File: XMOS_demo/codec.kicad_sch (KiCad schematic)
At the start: 1 part, among them U2 CS4271

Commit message: Lots of sch work
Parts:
- added C37, C39, C45, C47, C50: 100n, Capacitor_SMD:C_0603_1608Metric, symbol Device:C_Small
- added C43: 1u, Capacitor_SMD:CP_Elec_4x5.4, symbol Device:C_Polarized_Small
- added C44: 47u, Capacitor_SMD:CP_Elec_6.3x5.7, symbol Device:C_Polarized_Small
- added C46, C48, C49: 1u, Capacitor_SMD:C_0603_1608Metric, symbol Device:C_Small
- added R25, R28, R30, R31, R32, R33, R34: 0R, Resistor_SMD:R_0603_1608Metric, symbol Device:R_Small
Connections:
- net P3V3: now reaches U2.10 (VL)
- net P3V3: now also U2.9 (VD), C47.1, C48.1, C49.1, C50.1
- net ~{RST}: now reaches U2.14 (~{RST})
- net ~{RST}: now also R34.2
- net VQ1: now reaches U2.15 (VQ1)
- net VQ1: now also C39.1, C43.1
- net VQ2: now reaches U2.16 (VQ2)
- net AIN_A: now reaches U2.17 (AINA)
- net AIN_B: now reaches U2.18 (AINB)
- net VQ3: now reaches U2.19 (VQ3)
- net at U2.20 (VA): now also C45.1, C46.1, R25.1
- net GND: now reaches U2.21 (AGND)
- net GND: now also U2.8 (DGND), C37.2, C39.2, C43.2, C44.2, C45.2, C46.2, C47.2, C48.2, C49.2, C50.2
- net at U2.22 (FILT+): now also C37.1, C44.1
- net ~{MUTE}: now reaches U2.23 (~{AMUTEC})
- net OUT_A-: now reaches U2.24 (AOUTA-)
- net OUT_A+: now reaches U2.25 (AOUTA+)
- net OUT_B+: now reaches U2.26 (AOUTB+)
- net OUT_B-: now reaches U2.27 (AOUTB-)
- net MCLK: now reaches U2.3 (MCLK)
- net MCLK: now also R28.2
- net LRCK: now reaches U2.4 (LRCK)
- net LRCK: now also R30.2
- net SCLK: now reaches U2.5 (SCLK)
- net SCLK: now also R31.2
- net SDOUT: now reaches U2.6 (SDOUT(M/~{S}))
- net SDOUT: now also R33.2
- net SDIN: now reaches U2.7 (SDIN)
- net SDIN: now also R32.2
- new net CODEC_LRCK: R30.1
- new net CODEC_MCLK: R28.1
- new net CODEC_SCLK: R31.1
- new net CODEC_SDIN: R32.1
- new net CODEC_SDOUT: R33.1
- new net CODEC_~{RST}: R34.1
- new net P5V0: R25.2
- no-connect marks 0 -> 1
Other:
- note added: "TODO: DNP crystal, M/~{S} selection"
- moved on the sheet: U2

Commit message: sch work, pcb import and initial board outline
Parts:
- added C52, C53: 39p, Capacitor_SMD:C_0603_1608Metric, symbol Device:C_Small
- added R38, R40: 0R, Resistor_SMD:R_0603_1608Metric, symbol Device:R_Small
- added R39: 47k, Resistor_SMD:R_0603_1608Metric, symbol Device:R_Small
- added R43, R44: 680R, Resistor_SMD:R_0603_1608Metric, symbol Device:R_Small
- added Y2: 24.576M, Crystal:Crystal_SMD_2520-4Pin_2.5x2.0mm, symbol _Oscillator:Crystal_24M
- R25: value 0R -> 100k; Tolerance (none) -> 1%
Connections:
- net GND: now also R25.2, C52.2, C53.2, R38.1, R44.2, Y2.2 (G), Y2.4 (G)
- net P3V3: now also R39.1, R43.1
- net P5V0: now also R40.2; no longer R25.2
- net SDOUT: now also R39.2
- net ~{RST}: now also R25.1
- net at C45.1, C46.1, U2.20 (VA): now also R40.1; no longer R25.1
- net at U2.1 (XT0): now also C52.1, Y2.3
- net SCL: now reaches U2.11 (SCL/CCLK(M0))
- net SDA: now reaches U2.12 (SDA/CDIN(M1))
- net AD0: now reaches U2.13 (AD0/~{CS}(I2S/~{LJ}))
- net AD0: now also R43.2, R44.1
- net at U2.2 (XTI): now also C53.1, R38.2, Y2.1
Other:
- note removed: "TODO: DNP crystal, M/~{S} selection"
- moved on the sheet: C37, C39, C43, C44, R28, R30, R31, R32, R33, R34

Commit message: sch mostly finished, needs tp, pcb component layout started
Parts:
- renumbered C49 to C45, C50 to C46, C48 to C47, C47 to C48, C45 to C49, C46 to C50, C37 to C51, C44 to C52, C39 to C53, C43 to C54, C52 to C55, C53 to C56, R40 to R37, R34 to R38, R25 to R39, R28 to R40, R39 to R41, R30 to R42, R31 to R43, R33 to R44, R32 to R45, R43 to R46, R44 to R47, R38 to R48, U2 to U8

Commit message: finished sch, pcb work
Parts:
- renumbered R37 to R35, R38 to R36, R39 to R37, R40 to R38, R41 to R39, R42 to R40, R43 to R41, R44 to R42, R45 to R43, R46 to R44, R47 to R45, R48 to R46
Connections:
- net CODEC_MCLK is gone; now on net MCLK: R38.1
- net CODEC_LRCK renamed I2S_LRCK
- net CODEC_SCLK renamed I2S_SCLK
- net CODEC_SDIN renamed I2S_DAC
- net CODEC_SDOUT renamed I2S_ADC

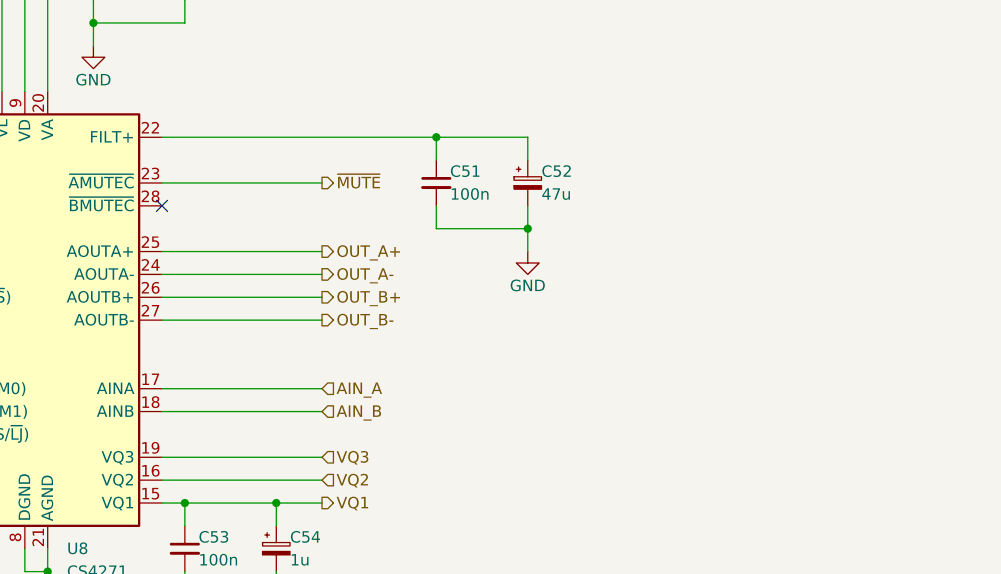
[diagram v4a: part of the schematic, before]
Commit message: sch work changes (jumpers, connectors, tp)
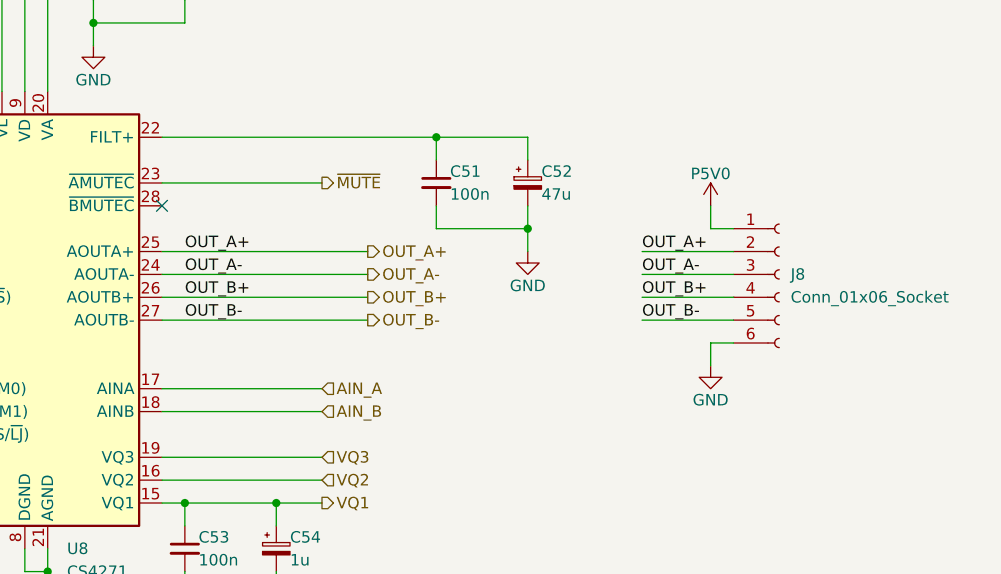
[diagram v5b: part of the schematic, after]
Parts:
- added J8: Conn_01x06_Socket, Connector_PinHeader_2.54mm:PinHeader_1x06_P2.54mm_Vertical, symbol Connector:Conn_01x06_Socket
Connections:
- net GND: now also J8.6 (Pin_6)
- net OUT_A+: now also J8.2 (Pin_2)
- net OUT_A-: now also J8.3 (Pin_3)
- net OUT_B+: now also J8.4 (Pin_4)
- net OUT_B-: now also J8.5 (Pin_5)
- net P5V0: now also J8.1 (Pin_1)

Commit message: merge
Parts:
- C46, C48, C49: footprint Capacitor_SMD:C_0603_1608Metric -> Capacitor_SMD:C_0402_1005Metric
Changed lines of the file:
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@@
 			)
 		)
-		(property "Footprint" "Capacitor_SMD:C_0603_1608Metric"
+		(property "Footprint" "Capacitor_SMD:C_0402_1005Metric"
 			(at 142.24 71.12 0)
 			(effects
@@
 			)
 		)
-		(property "Footprint" "Capacitor_SMD:C_0603_1608Metric"
+		(property "Footprint" "Capacitor_SMD:C_0402_1005Metric"
 			(at 157.48 71.12 0)
 			(effects
@@
 			)
 		)
-		(property "Footprint" "Capacitor_SMD:C_0603_1608Metric"
+		(property "Footprint" "Capacitor_SMD:C_0402_1005Metric"
 			(at 121.92 71.12 0)
 			(effects

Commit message: pcb routing
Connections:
- net VQ3 is gone; now on net VQ2_3: U8.19 (VQ3)
- net VQ2 renamed VQ2_3
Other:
- moved on the sheet: C45, C46, C47, C48, C49, C50, C51, C52, C53, C54, C55, C56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

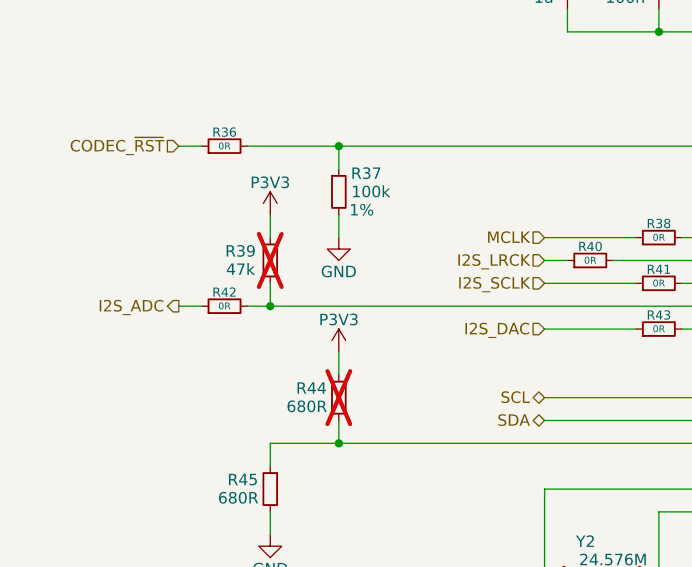
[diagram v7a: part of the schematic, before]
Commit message: I2S config sch page added
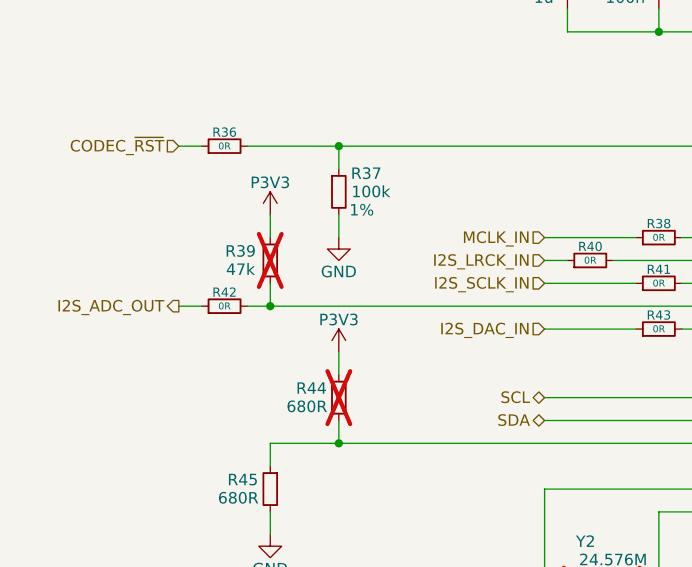
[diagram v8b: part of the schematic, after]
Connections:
- net MCLK: no longer R38.1
- net I2S_ADC renamed I2S_ADC_OUT
- net I2S_DAC renamed I2S_DAC_IN
- net I2S_LRCK renamed I2S_LRCK_IN
- net I2S_SCLK renamed I2S_SCLK_IN
- new net MCLK_IN: R38.1
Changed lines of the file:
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@@
 		)
 	)
-	(hierarchical_label "MCLK"
+	(hierarchical_label "MCLK_IN"
 		(shape input)
 		(at 208.28 137.16 180)
@@
 		)
 	)
-	(hierarchical_label "I2S_DAC"
+	(hierarchical_label "I2S_DAC_IN"
 		(shape input)
 		(at 208.28 147.32 180)
@@
 		)
 	)
-	(hierarchical_label "I2S_SCLK"
+	(hierarchical_label "I2S_SCLK_IN"
 		(shape input)
 		(at 208.28 142.24 180)
@@
 		)
 	)
-	(hierarchical_label "I2S_LRCK"
+	(hierarchical_label "I2S_LRCK_IN"
 		(shape input)
 		(at 208.28 139.7 180)
@@
 		)
 	)
-	(hierarchical_label "I2S_ADC"
+	(hierarchical_label "I2S_ADC_OUT"
 		(shape output)
 		(at 167.64 144.78 180)
